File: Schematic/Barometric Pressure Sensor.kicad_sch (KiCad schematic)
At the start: 8 parts, among them J17 BMP_INT, U20 BMP585

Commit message: 1st Schematic Review
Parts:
- renumbered C187 to C189, C189 to C190, C190 to C191, D48 to D47, J17 to J21, R156 to R148, U20 to U23
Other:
- note added: "MAX current draw is 260uA"
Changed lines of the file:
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@@
 		)
 	)
+	(text "MAX current draw is 260uA"
+		(exclude_from_sim no)
+		(at 141.986 118.364 0)
+		(effects
+			(font
+				(size 1.27 1.27)
+			)
+		)
+	)
 	(text "Per the datasheet, the unused INT pin is tied to GND to prevent a floating input.\nCRITICAL: The interrupt pin must be disabled in software to prevent a short circuit.\nEnsure the 'int_en' bit in the INT_CONFIG register (0x14) remains disabled (set to 0).\n\n\nDatasheet sets the IRQ to 0 on start up, so never turn it on\nPAGE49: 0x14 on reset is set to 0x35\nPAGE49: <int_en 2bits> <int_od 2bits> <int_pol 2bits> <int_mode 2bits LSB>\nPAGE51: 8.5, setup for 0x14, <0> <1> <0> <1>\nthis means: int_mode = latched, int_pol = active low, int_od = open_drain, int_en = disabled\nINT_CONFIG.int_en = 0\nINT_CONFIG.od = 1\nINT_CONFIG.pol = 0\nINT_CONFIG.mode = 1\nINT_CONFIG.pad_int_drv = 3"
 		(exclude_from_sim no)
@@
 		(on_board yes)
 		(dnp no)
-		(property "Reference" "R156"
+		(property "Reference" "R148"
 			(at 92.964 109.728 0)
 			(effects
@@
 			(project "STAR"
 				(path "/fc8533bc-25dd-4c20-9b4c-ffebebd6739b/93231d0a-659f-4d39-8e8d-78b96a3896a1/525f2b83-8347-468d-b8c8-5a1df0e1c532"
-					(reference "R156")
+					(reference "R148")
 					(unit 1)
 				)
@@
 		(on_board yes)
 		(dnp no)
-		(property "Reference" "#PWR096"
+		(property "Reference" "#PWR0100"
 			(at 166.37 137.16 0)
 			(effects
@@
 			(project "STAR"
 				(path "/fc8533bc-25dd-4c20-9b4c-ffebebd6739b/93231d0a-659f-4d39-8e8d-78b96a3896a1/525f2b83-8347-468d-b8c8-5a1df0e1c532"
-					(reference "#PWR096")
+					(reference "#PWR0100")
 					(unit 1)
 				)
@@
 		(on_board yes)
 		(dnp no)
-		(property "Reference" "J17"
+		(property "Reference" "J21"
 			(at 186.944 147.574 0)
 			(effects
@@
 			(project ""
 				(path "/fc8533bc-25dd-4c20-9b4c-ffebebd6739b/93231d0a-659f-4d39-8e8d-78b96a3896a1/525f2b83-8347-468d-b8c8-5a1df0e1c532"
-					(reference "J17")
+					(reference "J21")
 					(unit 1)
 				)
@@
 		(on_board yes)
 		(dnp no)
-		(property "Reference" "C187"
+		(property "Reference" "C189"
 			(at 115.824 110.998 0)
 			(effects
@@
 			(project "STAR"
 				(path "/fc8533bc-25dd-4c20-9b4c-ffebebd6739b/93231d0a-659f-4d39-8e8d-78b96a3896a1/525f2b83-8347-468d-b8c8-5a1df0e1c532"
-					(reference "C187")
+					(reference "C189")
 					(unit 1)
 				)
@@
 		(on_board yes)
 		(dnp no)
-		(property "Reference" "C189"
+		(property "Reference" "C190"
 			(at 180.594 105.918 0)
 			(effects
@@
 			(project "STAR"
 				(path "/fc8533bc-25dd-4c20-9b4c-ffebebd6739b/93231d0a-659f-4d39-8e8d-78b96a3896a1/525f2b83-8347-468d-b8c8-5a1df0e1c532"
-					(reference "C189")
+					(reference "C190")
 					(unit 1)
 				)
@@
 		(on_board yes)
 		(dnp no)
-		(property "Reference" "C190"
+		(property "Reference" "C191"
 			(at 188.214 105.918 0)
 			(effects
@@
 			(project "STAR"
 				(path "/fc8533bc-25dd-4c20-9b4c-ffebebd6739b/93231d0a-659f-4d39-8e8d-78b96a3896a1/525f2b83-8347-468d-b8c8-5a1df0e1c532"
-					(reference "C190")
+					(reference "C191")
 					(unit 1)
 				)
@@
 		(on_board yes)
 		(dnp no)
-		(property "Reference" "U20"
+		(property "Reference" "U23"
 			(at 151.892 94.234 0)
 			(effects
@@
 			(project "STAR"
 				(path "/fc8533bc-25dd-4c20-9b4c-ffebebd6739b/93231d0a-659f-4d39-8e8d-78b96a3896a1/525f2b83-8347-468d-b8c8-5a1df0e1c532"
-					(reference "U20")
+					(reference "U23")
 					(unit 1)
 				)
@@
 		(on_board yes)
 		(dnp no)
-		(property "Reference" "D48"
+		(property "Reference" "D47"
 			(at 94.234 120.904 90)
 			(effects
@@
 			(project "STAR"
 				(path "/fc8533bc-25dd-4c20-9b4c-ffebebd6739b/93231d0a-659f-4d39-8e8d-78b96a3896a1/525f2b83-8347-468d-b8c8-5a1df0e1c532"
-					(reference "D48")
+					(reference "D47")
 					(unit 1)
 				)

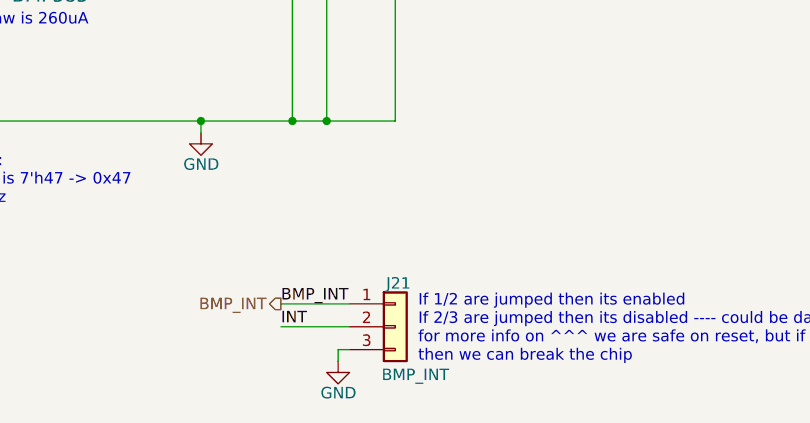
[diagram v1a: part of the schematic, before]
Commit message: added so many test points
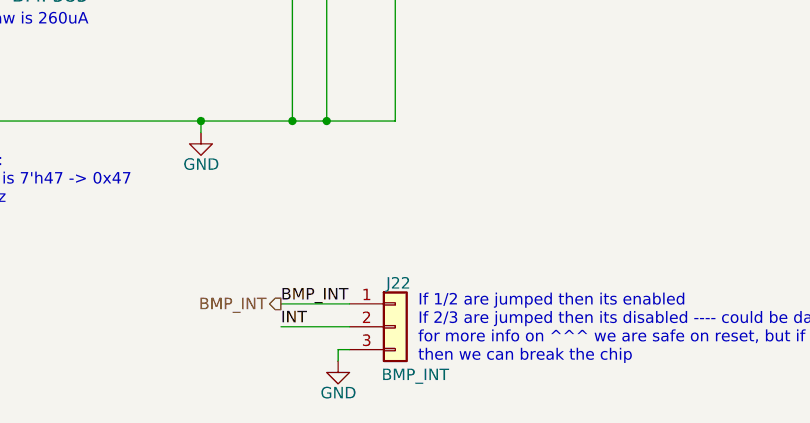
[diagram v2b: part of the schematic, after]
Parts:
- renumbered J21 to J22
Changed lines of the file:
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@@
 		(on_board yes)
 		(dnp no)
-		(property "Reference" "#PWR0100"
+		(property "Reference" "#PWR0101"
 			(at 166.37 137.16 0)
 			(effects
@@
 			(project "STAR"
 				(path "/fc8533bc-25dd-4c20-9b4c-ffebebd6739b/93231d0a-659f-4d39-8e8d-78b96a3896a1/525f2b83-8347-468d-b8c8-5a1df0e1c532"
-					(reference "#PWR0100")
+					(reference "#PWR0101")
 					(unit 1)
 				)
@@
 		(on_board yes)
 		(dnp no)
-		(property "Reference" "J21"
+		(property "Reference" "J22"
 			(at 186.944 147.574 0)
 			(effects
@@
 			(project ""
 				(path "/fc8533bc-25dd-4c20-9b4c-ffebebd6739b/93231d0a-659f-4d39-8e8d-78b96a3896a1/525f2b83-8347-468d-b8c8-5a1df0e1c532"
-					(reference "J21")
+					(reference "J22")
 					(unit 1)
 				)
@@
 		(on_board yes)
 		(dnp no)
-		(property "Reference" "#PWR0101"
+		(property "Reference" "#PWR0102"
 			(at 181.61 162.56 0)
 			(effects
@@
 			(project "STAR"
 				(path "/fc8533bc-25dd-4c20-9b4c-ffebebd6739b/93231d0a-659f-4d39-8e8d-78b96a3896a1/525f2b83-8347-468d-b8c8-5a1df0e1c532"
-					(reference "#PWR0101")
+					(reference "#PWR0102")
 					(unit 1)
 				)

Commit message: updates
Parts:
- renumbered C188 to C190, C189 to C191, C190 to C192, C191 to C193, D47 to D49, J22 to J24, R148 to R161
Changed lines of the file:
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@@
 		(on_board yes)
 		(dnp no)
-		(property "Reference" "R148"
+		(property "Reference" "R161"
 			(at 92.964 109.728 0)
 			(effects
@@
 			(project "STAR"
 				(path "/fc8533bc-25dd-4c20-9b4c-ffebebd6739b/93231d0a-659f-4d39-8e8d-78b96a3896a1/525f2b83-8347-468d-b8c8-5a1df0e1c532"
-					(reference "R148")
+					(reference "R161")
 					(unit 1)
 				)
@@
 		(on_board yes)
 		(dnp no)
-		(property "Reference" "C188"
+		(property "Reference" "C190"
 			(at 108.204 110.998 0)
 			(effects
@@
 			(project "STAR"
 				(path "/fc8533bc-25dd-4c20-9b4c-ffebebd6739b/93231d0a-659f-4d39-8e8d-78b96a3896a1/525f2b83-8347-468d-b8c8-5a1df0e1c532"
-					(reference "C188")
+					(reference "C190")
 					(unit 1)
 				)
@@
 		(on_board yes)
 		(dnp no)
-		(property "Reference" "#PWR0101"
+		(property "Reference" "#PWR0103"
 			(at 166.37 137.16 0)
 			(effects
@@
 			(project "STAR"
 				(path "/fc8533bc-25dd-4c20-9b4c-ffebebd6739b/93231d0a-659f-4d39-8e8d-78b96a3896a1/525f2b83-8347-468d-b8c8-5a1df0e1c532"
-					(reference "#PWR0101")
+					(reference "#PWR0103")
 					(unit 1)
 				)
@@
 		(on_board yes)
 		(dnp no)
-		(property "Reference" "J22"
+		(property "Reference" "J24"
 			(at 186.944 147.574 0)
 			(effects
@@
 			(project ""
 				(path "/fc8533bc-25dd-4c20-9b4c-ffebebd6739b/93231d0a-659f-4d39-8e8d-78b96a3896a1/525f2b83-8347-468d-b8c8-5a1df0e1c532"
-					(reference "J22")
+					(reference "J24")
 					(unit 1)
 				)
@@
 		(on_board yes)
 		(dnp no)
-		(property "Reference" "C189"
+		(property "Reference" "C191"
 			(at 115.824 110.998 0)
 			(effects
@@
 			(project "STAR"
 				(path "/fc8533bc-25dd-4c20-9b4c-ffebebd6739b/93231d0a-659f-4d39-8e8d-78b96a3896a1/525f2b83-8347-468d-b8c8-5a1df0e1c532"
-					(reference "C189")
+					(reference "C191")
 					(unit 1)
 				)
@@
 		(on_board yes)
 		(dnp no)
-		(property "Reference" "C190"
+		(property "Reference" "C192"
 			(at 180.594 105.918 0)
 			(effects
@@
 			(project "STAR"
 				(path "/fc8533bc-25dd-4c20-9b4c-ffebebd6739b/93231d0a-659f-4d39-8e8d-78b96a3896a1/525f2b83-8347-468d-b8c8-5a1df0e1c532"
-					(reference "C190")
+					(reference "C192")
 					(unit 1)
 				)
@@
 		(on_board yes)
 		(dnp no)
-		(property "Reference" "C191"
+		(property "Reference" "C193"
 			(at 188.214 105.918 0)
 			(effects
@@
 			(project "STAR"
 				(path "/fc8533bc-25dd-4c20-9b4c-ffebebd6739b/93231d0a-659f-4d39-8e8d-78b96a3896a1/525f2b83-8347-468d-b8c8-5a1df0e1c532"
-					(reference "C191")
+					(reference "C193")
 					(unit 1)
 				)
@@
 		(on_board yes)
 		(dnp no)
-		(property "Reference" "D47"
+		(property "Reference" "D49"
 			(at 94.234 120.904 90)
 			(effects
@@
 			(project "STAR"
 				(path "/fc8533bc-25dd-4c20-9b4c-ffebebd6739b/93231d0a-659f-4d39-8e8d-78b96a3896a1/525f2b83-8347-468d-b8c8-5a1df0e1c532"
-					(reference "D47")
+					(reference "D49")
 					(unit 1)
 				)
@@
 		(on_board yes)
 		(dnp no)
-		(property "Reference" "#PWR0102"
+		(property "Reference" "#PWR0104"
 			(at 181.61 162.56 0)
 			(effects
@@
 			(project "STAR"
 				(path "/fc8533bc-25dd-4c20-9b4c-ffebebd6739b/93231d0a-659f-4d39-8e8d-78b96a3896a1/525f2b83-8347-468d-b8c8-5a1df0e1c532"
-					(reference "#PWR0102")
+					(reference "#PWR0104")
 					(unit 1)
 				)

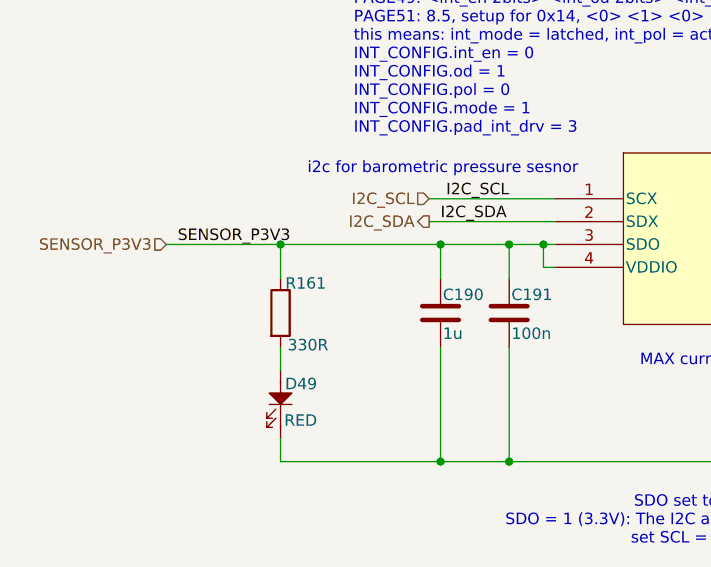
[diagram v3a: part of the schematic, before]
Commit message: updated fuel guage
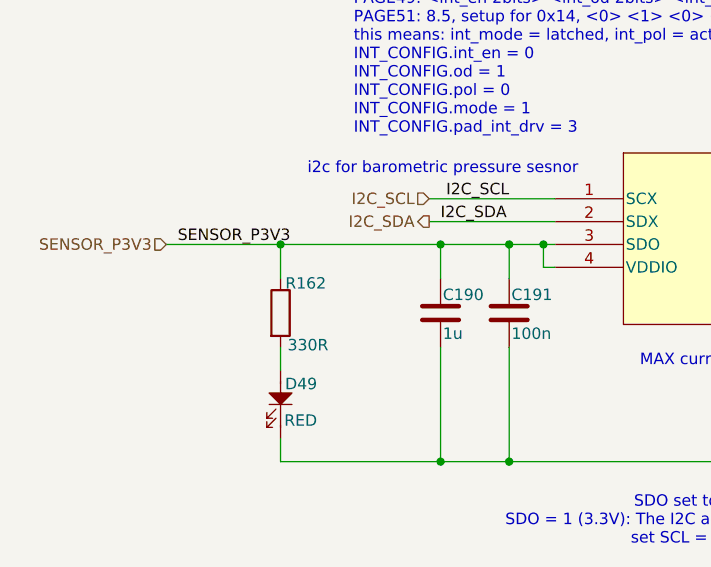
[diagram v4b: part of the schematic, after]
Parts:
- renumbered R161 to R162
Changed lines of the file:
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@@
 		(on_board yes)
 		(dnp no)
-		(property "Reference" "R161"
+		(property "Reference" "R162"
 			(at 92.964 109.728 0)
 			(effects
@@
 			(project "STAR"
 				(path "/fc8533bc-25dd-4c20-9b4c-ffebebd6739b/93231d0a-659f-4d39-8e8d-78b96a3896a1/525f2b83-8347-468d-b8c8-5a1df0e1c532"
-					(reference "R161")
+					(reference "R162")
 					(unit 1)
 				)

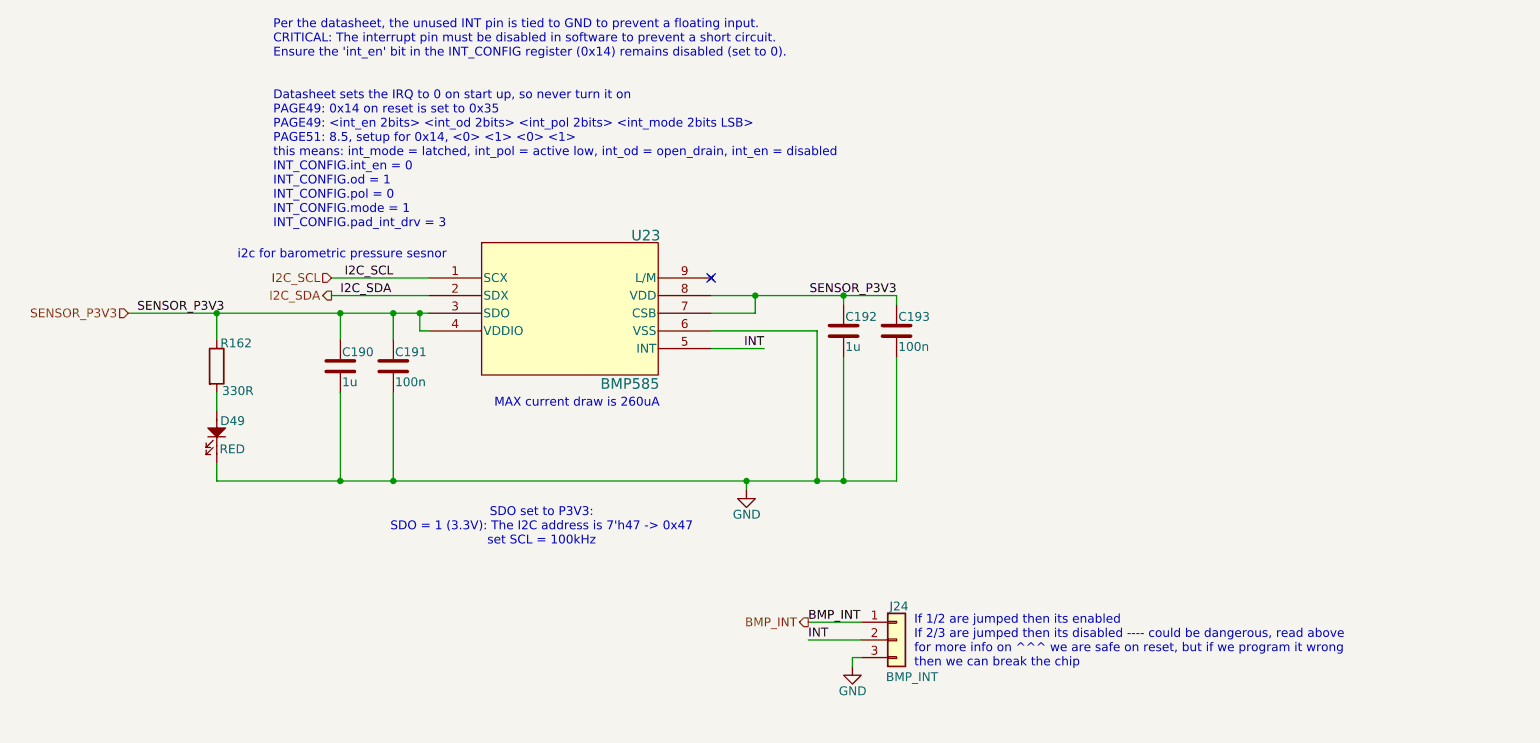
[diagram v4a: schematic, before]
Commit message: Added MCU
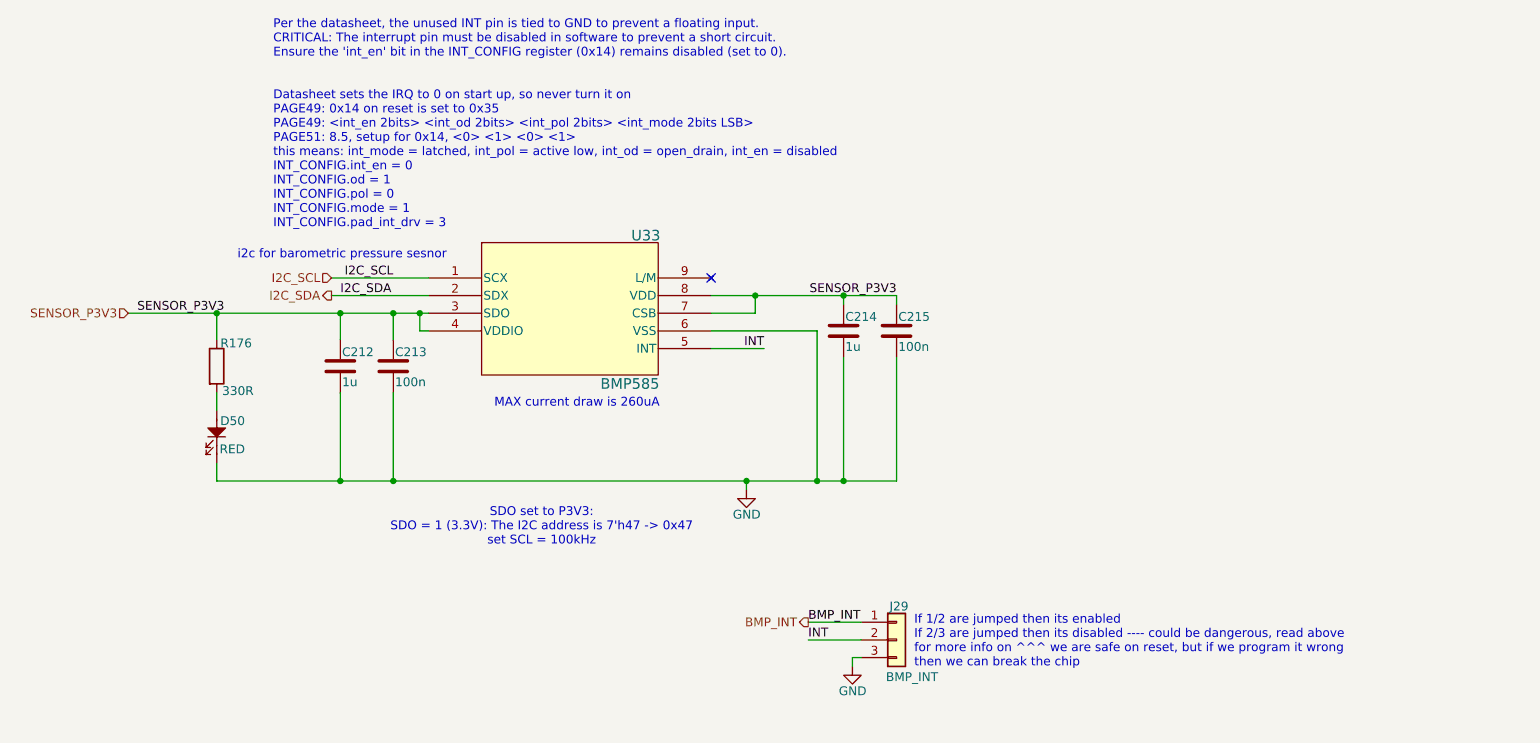
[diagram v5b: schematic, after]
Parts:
- renumbered C190 to C212, C191 to C213, C192 to C214, C193 to C215, D49 to D50, J24 to J29, R162 to R176, U23 to U33
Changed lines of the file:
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@@
 		(on_board yes)
 		(dnp no)
-		(property "Reference" "R162"
+		(property "Reference" "R176"
 			(at 92.964 109.728 0)
 			(effects
@@
 			(project "STAR"
 				(path "/fc8533bc-25dd-4c20-9b4c-ffebebd6739b/93231d0a-659f-4d39-8e8d-78b96a3896a1/525f2b83-8347-468d-b8c8-5a1df0e1c532"
-					(reference "R162")
+					(reference "R176")
 					(unit 1)
 				)
@@
 		(on_board yes)
 		(dnp no)
-		(property "Reference" "C190"
+		(property "Reference" "C212"
 			(at 108.204 110.998 0)
 			(effects
@@
 			(project "STAR"
 				(path "/fc8533bc-25dd-4c20-9b4c-ffebebd6739b/93231d0a-659f-4d39-8e8d-78b96a3896a1/525f2b83-8347-468d-b8c8-5a1df0e1c532"
-					(reference "C190")
+					(reference "C212")
 					(unit 1)
 				)
@@
 		(on_board yes)
 		(dnp no)
-		(property "Reference" "#PWR0103"
+		(property "Reference" "#PWR0115"
 			(at 166.37 137.16 0)
 			(effects
@@
 			(project "STAR"
 				(path "/fc8533bc-25dd-4c20-9b4c-ffebebd6739b/93231d0a-659f-4d39-8e8d-78b96a3896a1/525f2b83-8347-468d-b8c8-5a1df0e1c532"
-					(reference "#PWR0103")
+					(reference "#PWR0115")
 					(unit 1)
 				)
@@
 		(on_board yes)
 		(dnp no)
-		(property "Reference" "J24"
+		(property "Reference" "J29"
 			(at 186.944 147.574 0)
 			(effects
@@
 			(project ""
 				(path "/fc8533bc-25dd-4c20-9b4c-ffebebd6739b/93231d0a-659f-4d39-8e8d-78b96a3896a1/525f2b83-8347-468d-b8c8-5a1df0e1c532"
-					(reference "J24")
+					(reference "J29")
 					(unit 1)
 				)
@@
 		(on_board yes)
 		(dnp no)
-		(property "Reference" "C191"
+		(property "Reference" "C213"
 			(at 115.824 110.998 0)
 			(effects
@@
 			(project "STAR"
 				(path "/fc8533bc-25dd-4c20-9b4c-ffebebd6739b/93231d0a-659f-4d39-8e8d-78b96a3896a1/525f2b83-8347-468d-b8c8-5a1df0e1c532"
-					(reference "C191")
+					(reference "C213")
 					(unit 1)
 				)
@@
 		(on_board yes)
 		(dnp no)
-		(property "Reference" "C192"
+		(property "Reference" "C214"
 			(at 180.594 105.918 0)
 			(effects
@@
 			(project "STAR"
 				(path "/fc8533bc-25dd-4c20-9b4c-ffebebd6739b/93231d0a-659f-4d39-8e8d-78b96a3896a1/525f2b83-8347-468d-b8c8-5a1df0e1c532"
-					(reference "C192")
+					(reference "C214")
 					(unit 1)
 				)
@@
 		(on_board yes)
 		(dnp no)
-		(property "Reference" "C193"
+		(property "Reference" "C215"
 			(at 188.214 105.918 0)
 			(effects
@@
 			(project "STAR"
 				(path "/fc8533bc-25dd-4c20-9b4c-ffebebd6739b/93231d0a-659f-4d39-8e8d-78b96a3896a1/525f2b83-8347-468d-b8c8-5a1df0e1c532"
-					(reference "C193")
+					(reference "C215")
 					(unit 1)
 				)
@@
 		(on_board yes)
 		(dnp no)
-		(property "Reference" "U23"
+		(property "Reference" "U33"
 			(at 151.892 94.234 0)
 			(effects
@@
 			(project "STAR"
 				(path "/fc8533bc-25dd-4c20-9b4c-ffebebd6739b/93231d0a-659f-4d39-8e8d-78b96a3896a1/525f2b83-8347-468d-b8c8-5a1df0e1c532"
-					(reference "U23")
+					(reference "U33")
 					(unit 1)
 				)
@@
 		(on_board yes)
 		(dnp no)
-		(property "Reference" "D49"
+		(property "Reference" "D50"
 			(at 94.234 120.904 90)
 			(effects
@@
 			(project "STAR"
 				(path "/fc8533bc-25dd-4c20-9b4c-ffebebd6739b/93231d0a-659f-4d39-8e8d-78b96a3896a1/525f2b83-8347-468d-b8c8-5a1df0e1c532"
-					(reference "D49")
+					(reference "D50")
 					(unit 1)
 				)
@@
 		(on_board yes)
 		(dnp no)
-		(property "Reference" "#PWR0104"
+		(property "Reference" "#PWR0116"
 			(at 181.61 162.56 0)
 			(effects
@@
 			(project "STAR"
 				(path "/fc8533bc-25dd-4c20-9b4c-ffebebd6739b/93231d0a-659f-4d39-8e8d-78b96a3896a1/525f2b83-8347-468d-b8c8-5a1df0e1c532"
-					(reference "#PWR0104")
+					(reference "#PWR0116")
 					(unit 1)
 				)

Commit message: Started to work on the BOM
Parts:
- added TP153: TestPoint, symbol Connector:TestPoint
- C208: renamed from C212; footprint (none) -> Capacitor_SMD:C_1206_3216Metric_Pad1.33x1.80mm_HandSolder; Link (none) -> https://mou.sr/41y0aEA; Manufacturer Part Number (none) -> CL31B105KBHNNNE; Price per Unit (none) -> 0.11; Supplier (none) -> Mouser; Supplier Part Number (none) -> 187-CL31B105KBHNNNE; now not fitted; now left out of the parts list
- C209: renamed from C213; footprint (none) -> Capacitor_SMD:C_1206_3216Metric_Pad1.33x1.80mm_HandSolder; Link (none) -> https://mou.sr/4n9ybmQ; Manufacturer Part Number (none) -> CL31B104KBCNNNC; Price per Unit (none) -> 0.11; Supplier (none) -> Mouser; Supplier Part Number (none) -> 187-CL31B104KBCNNNC; now not fitted; now left out of the parts list
- C210: renamed from C214; footprint (none) -> Capacitor_SMD:C_1206_3216Metric_Pad1.33x1.80mm_HandSolder; Link (none) -> https://mou.sr/41y0aEA; Manufacturer Part Number (none) -> CL31B105KBHNNNE; Price per Unit (none) -> 0.11; Supplier (none) -> Mouser; Supplier Part Number (none) -> 187-CL31B105KBHNNNE; now not fitted; now left out of the parts list
- C211: renamed from C215; footprint (none) -> Capacitor_SMD:C_1206_3216Metric_Pad1.33x1.80mm_HandSolder; Link (none) -> https://mou.sr/4n9ybmQ; Manufacturer Part Number (none) -> CL31B104KBCNNNC; Price per Unit (none) -> 0.11; Supplier (none) -> Mouser; Supplier Part Number (none) -> 187-CL31B104KBCNNNC; now not fitted; now left out of the parts list
- D47: renamed from D50; footprint PCM_Diode_SMD_AKL:D_0805_2012Metric -> ASMM-CR03-BU802:LEDM3528X210N; Link (none) -> https://mou.sr/460BFB7; Manufacturer Part Number (none) -> ASMM-CR03-BU802; Price per Unit (none) -> 0.32; Supplier (none) -> Mouser; Supplier Part Number (none) -> 630-ASMM-CR03-BU802; now not fitted; now left out of the parts list
- J27: renamed from J29; now not fitted; now left out of the parts list
- R172: renamed from R176; now not fitted; now left out of the parts list
- U31: renamed from U33; footprint LGA9_BMP585_BOS -> (none); now not fitted; now left out of the parts list
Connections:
- net BMP_INT: now also TP153.1
